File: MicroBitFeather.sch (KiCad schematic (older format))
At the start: 8 parts

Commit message: Wired some more things up.
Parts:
- added R?: 470, symbol R
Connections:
- net +5V: now also J?.1, U?.14 (VCC)
- net GND: now also J?.2, J?.MP (MountPin), U?.1 (~1OE), U?.10 (~3OE), U?.12 (4A), U?.13 (~4OE), U?.4 (~2OE), U?.5 (2A), U?.7 (GND), U?.9 (3A)
- net P1: now also U?.2 (1A)
- net at U?.3 (1Y): now also R?.1
- net at J?.2 (Pin_2): now also R?.2
- no-connect marks 1 -> 4
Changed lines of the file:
@@
 	1    0    0    -1
 $EndComp
+$Comp
+L +5V #PWR?
+U 1 1 5B87920C
+P 4700 4000
+F 0 "#PWR?" H 4700 3850 50  0001 C CNN
+F 1 "+5V" H 4700 4140 50  0000 C CNN
+F 2 "" H 4700 4000 50  0001 C CNN
+F 3 "" H 4700 4000 50  0001 C CNN
+	1    4700 4000
+	1    0    0    -1
+$EndComp
+$Comp
+L GND #PWR?
+U 1 1 5B879238
+P 4700 5600
+F 0 "#PWR?" H 4700 5350 50  0001 C CNN
+F 1 "GND" H 4700 5450 50  0000 C CNN
+F 2 "" H 4700 5600 50  0001 C CNN
+F 3 "" H 4700 5600 50  0001 C CNN
+	1    4700 5600
+	1    0    0    -1
+$EndComp
+Wire Wire Line
+	4700 4100 4700 4000
+Wire Wire Line
+	4700 5500 4700 5600
+$Comp
+L +5V #PWR?
+U 1 1 5B879F10
+P 4900 6000
+F 0 "#PWR?" H 4900 5850 50  0001 C CNN
+F 1 "+5V" H 4900 6140 50  0000 C CNN
+F 2 "" H 4900 6000 50  0001 C CNN
+F 3 "" H 4900 6000 50  0001 C CNN
+	1    4900 6000
+	1    0    0    -1
+$EndComp
+$Comp
+L GND #PWR?
+U 1 1 5B879F3C
+P 4500 6700
+F 0 "#PWR?" H 4500 6450 50  0001 C CNN
+F 1 "GND" H 4500 6550 50  0000 C CNN
+F 2 "" H 4500 6700 50  0001 C CNN
+F 3 "" H 4500 6700 50  0001 C CNN
+	1    4500 6700
+	1    0    0    -1
+$EndComp
+Wire Wire Line
+	4800 6100 4900 6100
+Wire Wire Line
+	4900 6100 4900 6000
+Wire Wire Line
+	4500 6500 4500 6700
+Wire Wire Line
+	4800 6300 5500 6300
+Wire Wire Line
+	5500 6300 5500 6600
+Wire Wire Line
+	5500 6600 4500 6600
+Connection ~ 4500 6600
+Wire Wire Line
+	5100 4300 5500 4300
+Wire Wire Line
+	5500 4800 6200 4800
+Wire Wire Line
+	4300 4400 4200 4400
+Wire Wire Line
+	4200 4400 4200 5550
+Wire Wire Line
+	4200 5550 4700 5550
+Connection ~ 4700 5550
+Wire Wire Line
+	4300 4600 4200 4600
+Connection ~ 4200 4600
+Wire Wire Line
+	4300 4700 4200 4700
+Connection ~ 4200 4700
+Wire Wire Line
+	4300 4900 4200 4900
+Connection ~ 4200 4900
+Wire Wire Line
+	4300 5000 4200 5000
+Connection ~ 4200 5000
+Wire Wire Line
+	4300 5200 4200 5200
+Connection ~ 4200 5200
+Wire Wire Line
+	4300 5300 4200 5300
+Connection ~ 4200 5300
+Text Label 4000 4300 0    50   ~ 0
+P1
+Wire Wire Line
+	4000 4300 4300 4300
+NoConn ~ 5100 4600
+NoConn ~ 5100 4900
+NoConn ~ 5100 5200
+$Comp
+L R R?
+U 1 1 5B87B000
+P 5500 4550
+F 0 "R?" V 5580 4550 50  0000 C CNN
+F 1 "470" V 5500 4550 50  0000 C CNN
+F 2 "" V 5430 4550 50  0001 C CNN
+F 3 "" H 5500 4550 50  0001 C CNN
+	1    5500 4550
+	1    0    0    -1
+$EndComp
+Wire Wire Line
+	5500 4300 5500 4400
+Wire Wire Line
+	5500 4700 5500 4800
 $EndSCHEMATC

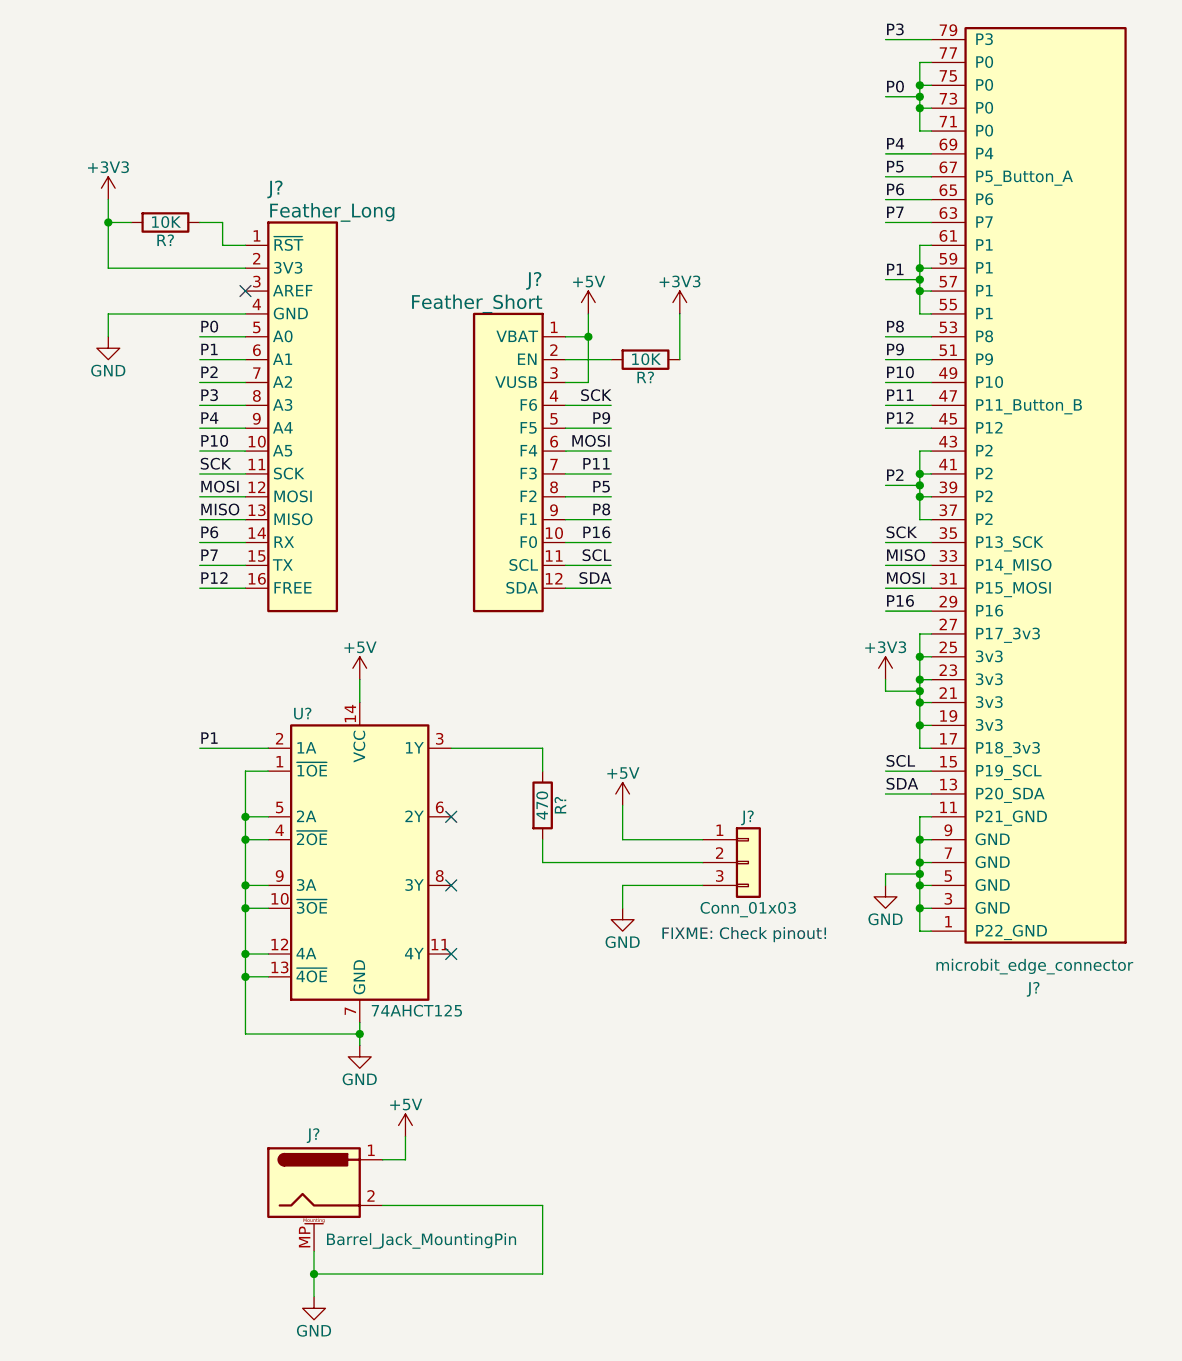
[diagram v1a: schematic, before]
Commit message: Add voltage regulator and more.
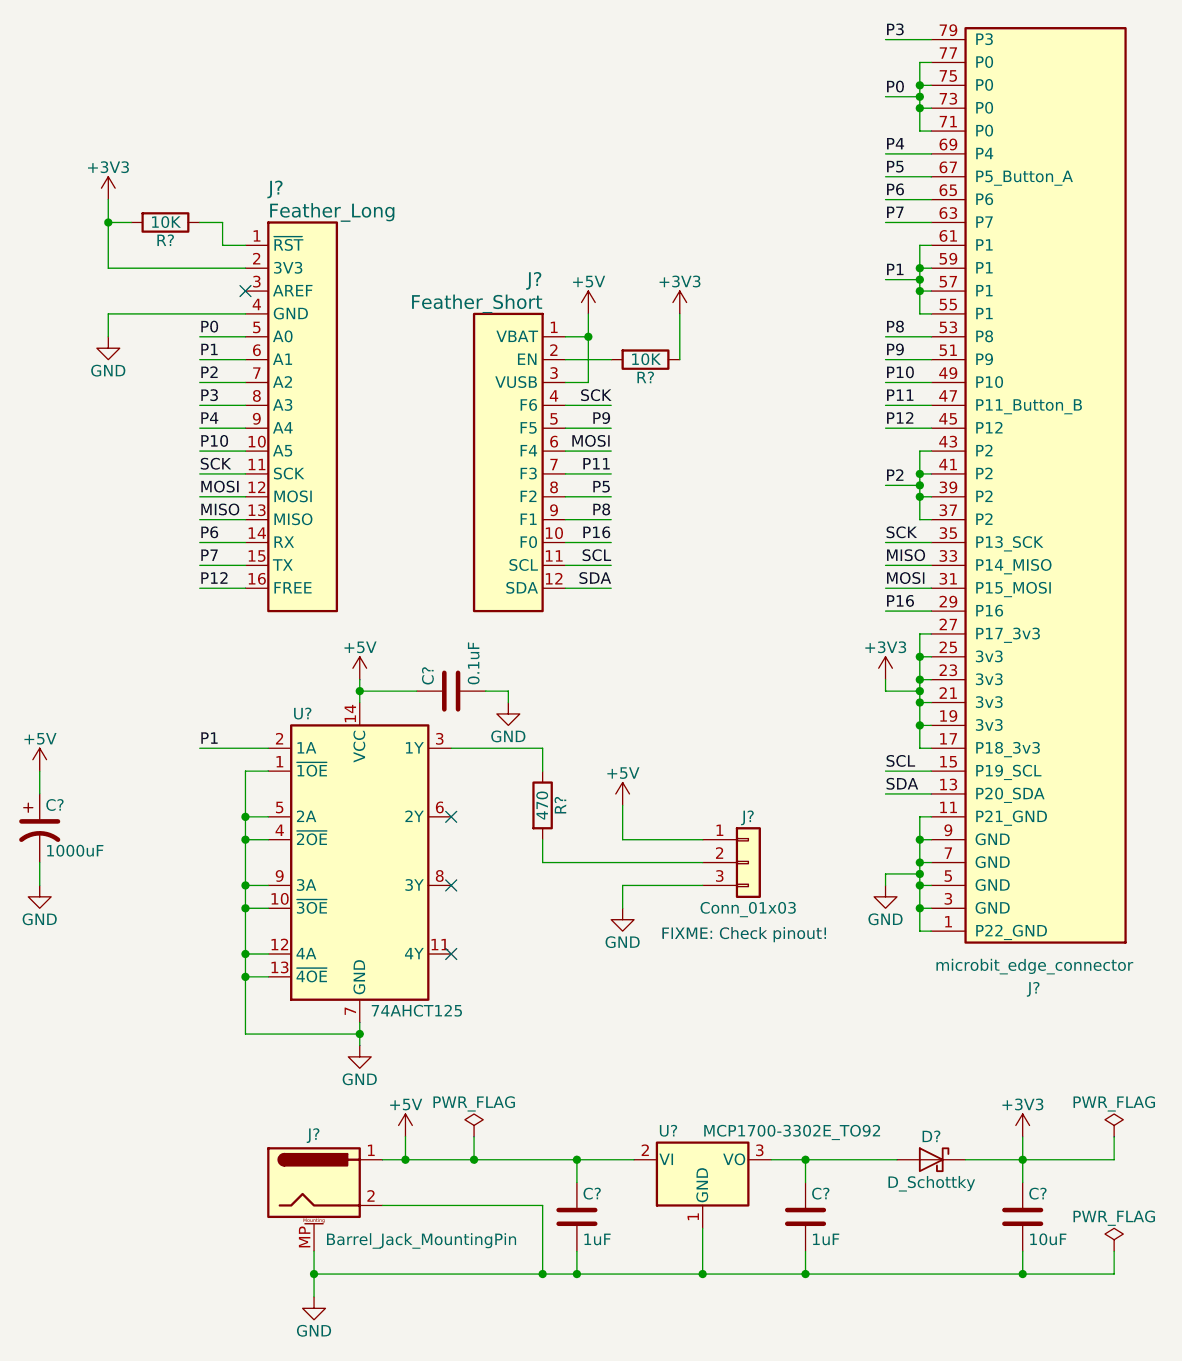
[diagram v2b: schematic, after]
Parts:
- added C? (x2): 1uF, symbol C
- added C?: 10uF, symbol C
- added C?: 0.1uF, symbol C
- added C?: 1000uF, symbol CP1
- added D?: D_Schottky, symbol D_Schottky
- added U?: MCP1700-3302E_TO92, TO_SOT_Packages_THT:TO-92_Inline_Narrow_Oval, symbol MCP1700-3302E_TO92
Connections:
- net +3V3: now also C?.1, D?.1 (K)
- net +5V: now also C?.1, C?.1, C?.1, U?.2 (VI)
- net GND: now also C?.2, C?.2, C?.2, C?.2, C?.2, U?.1 (GND)
- new net: C?.1, D?.2 (A), U?.3 (VO)
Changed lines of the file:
@@
 $EndComp
 Wire Wire Line
-	4800 6100 4900 6100
+	4800 6100 5900 6100
 Wire Wire Line
 	4900 6100 4900 6000
@@
 	5500 6300 5500 6600
 Wire Wire Line
-	5500 6600 4500 6600
+	4500 6600 8000 6600
 Connection ~ 4500 6600
 Wire Wire Line
@@
 Wire Wire Line
 	5500 4700 5500 4800
+$Comp
+L MCP1700-3302E_TO92 U?
+U 1 1 5B87B6E7
+P 6200 6100
+F 0 "U?" H 6050 5975 50  0000 C CNN
+F 1 "MCP1700-3302E_TO92" H 6200 5975 50  0000 L CNN
+F 2 "TO_SOT_Packages_THT:TO-92_Inline_Narrow_Oval" H 6200 5900 50  0001 C CIN
+F 3 "" H 6200 6100 50  0001 C CNN
+	1    6200 6100
+	1    0    0    1
+$EndComp
+$Comp
+L C C?
+U 1 1 5B87B8CD
+P 5650 6350
+F 0 "C?" H 5675 6450 50  0000 L CNN
+F 1 "1uF" H 5675 6250 50  0000 L CNN
+F 2 "" H 5688 6200 50  0001 C CNN
+F 3 "" H 5650 6350 50  0001 C CNN
+	1    5650 6350
+	1    0    0    -1
+$EndComp
+$Comp
+L C C?
+U 1 1 5B87B9B3
+P 6650 6350
+F 0 "C?" H 6675 6450 50  0000 L CNN
+F 1 "1uF" H 6675 6250 50  0000 L CNN
+F 2 "" H 6688 6200 50  0001 C CNN
+F 3 "" H 6650 6350 50  0001 C CNN
+	1    6650 6350
+	1    0    0    -1
+$EndComp
+Connection ~ 4900 6100
+Wire Wire Line
+	6650 6600 6650 6500
+Connection ~ 5500 6600
+Wire Wire Line
+	5650 6500 5650 6600
+Connection ~ 5650 6600
+Wire Wire Line
+	6200 6400 6200 6600
+Connection ~ 6200 6600
+$Comp
+L +3V3 #PWR?
+U 1 1 5B87BEFA
+P 7600 6000
+F 0 "#PWR?" H 7600 5850 50  0001 C CNN
+F 1 "+3V3" H 7600 6140 50  0000 C CNN
+F 2 "" H 7600 6000 50  0001 C CNN
+F 3 "" H 7600 6000 50  0001 C CNN
+	1    7600 6000
+	1    0    0    -1
+$EndComp
+Wire Wire Line
+	6500 6100 7050 6100
+Wire Wire Line
+	6650 6100 6650 6200
+$Comp
+L D_Schottky D?
+U 1 1 5B87C03F
+P 7200 6100
+F 0 "D?" H 7200 6200 50  0000 C CNN
+F 1 "D_Schottky" H 7200 6000 50  0000 C CNN
+F 2 "" H 7200 6100 50  0001 C CNN
+F 3 "" H 7200 6100 50  0001 C CNN
+	1    7200 6100
+	-1   0    0    -1
+$EndComp
+Connection ~ 6650 6100
+Wire Wire Line
+	7350 6100 8000 6100
+Wire Wire Line
+	7600 6000 7600 6200
+$Comp
+L C C?
+U 1 1 5B87C55E
+P 7600 6350
+F 0 "C?" H 7625 6450 50  0000 L CNN
+F 1 "10uF" H 7625 6250 50  0000 L CNN
+F 2 "" H 7638 6200 50  0001 C CNN
+F 3 "" H 7600 6350 50  0001 C CNN
+	1    7600 6350
+	1    0    0    -1
+$EndComp
+Connection ~ 7600 6100
+Wire Wire Line
+	7600 6600 7600 6500
+Connection ~ 6650 6600
+Wire Wire Line
+	5650 6200 5650 6100
+Connection ~ 5650 6100
+$Comp
+L C C?
+U 1 1 5B87CADC
+P 5100 4050
+F 0 "C?" H 5125 4150 50  0000 L CNN
+F 1 "0.1uF" H 5125 3950 50  0000 L CNN
+F 2 "" H 5138 3900 50  0001 C CNN
+F 3 "" H 5100 4050 50  0001 C CNN
+	1    5100 4050
+	0    -1   -1   0
+$EndComp
+$Comp
+L GND #PWR?
+U 1 1 5B87CC46
+P 5350 4100
+F 0 "#PWR?" H 5350 3850 50  0001 C CNN
+F 1 "GND" H 5350 3950 50  0000 C CNN
+F 2 "" H 5350 4100 50  0001 C CNN
+F 3 "" H 5350 4100 50  0001 C CNN
+	1    5350 4100
+	1    0    0    -1
+$EndComp
+Wire Wire Line
+	4700 4050 4950 4050
+Connection ~ 4700 4050
+Wire Wire Line
+	5250 4050 5350 4050
+Wire Wire Line
+	5350 4050 5350 4100
+$Comp
+L CP1 C?
+U 1 1 5B87D36C
+P 3300 4650
+F 0 "C?" H 3325 4750 50  0000 L CNN
+F 1 "1000uF" H 3325 4550 50  0000 L CNN
+F 2 "" H 3300 4650 50  0001 C CNN
+F 3 "" H 3300 4650 50  0001 C CNN
+	1    3300 4650
+	1    0    0    -1
+$EndComp
+$Comp
+L GND #PWR?
+U 1 1 5B87D3B2
+P 3300 4900
+F 0 "#PWR?" H 3300 4650 50  0001 C CNN
+F 1 "GND" H 3300 4750 50  0000 C CNN
+F 2 "" H 3300 4900 50  0001 C CNN
+F 3 "" H 3300 4900 50  0001 C CNN
+	1    3300 4900
+	1    0    0    -1
+$EndComp
+$Comp
+L +5V #PWR?
+U 1 1 5B87D3F6
+P 3300 4400
+F 0 "#PWR?" H 3300 4250 50  0001 C CNN
+F 1 "+5V" H 3300 4540 50  0000 C CNN
+F 2 "" H 3300 4400 50  0001 C CNN
+F 3 "" H 3300 4400 50  0001 C CNN
+	1    3300 4400
+	1    0    0    -1
+$EndComp
+Wire Wire Line
+	3300 4500 3300 4400
+Wire Wire Line
+	3300 4800 3300 4900
+$Comp
+L PWR_FLAG #FLG?
+U 1 1 5B87DB70
+P 5200 6000
+F 0 "#FLG?" H 5200 6075 50  0001 C CNN
+F 1 "PWR_FLAG" H 5200 6150 50  0000 C CNN
+F 2 "" H 5200 6000 50  0001 C CNN
+F 3 "" H 5200 6000 50  0001 C CNN
+	1    5200 6000
+	1    0    0    -1
+$EndComp
+$Comp
+L PWR_FLAG #FLG?
+U 1 1 5B87DBB4
+P 8000 6000
+F 0 "#FLG?" H 8000 6075 50  0001 C CNN
+F 1 "PWR_FLAG" H 8000 6150 50  0000 C CNN
+F 2 "" H 8000 6000 50  0001 C CNN
+F 3 "" H 8000 6000 50  0001 C CNN
+	1    8000 6000
+	1    0    0    -1
+$EndComp
+$Comp
+L PWR_FLAG #FLG?
+U 1 1 5B87DBF8
+P 8000 6500
+F 0 "#FLG?" H 8000 6575 50  0001 C CNN
+F 1 "PWR_FLAG" H 8000 6650 50  0000 C CNN
+F 2 "" H 8000 6500 50  0001 C CNN
+F 3 "" H 8000 6500 50  0001 C CNN
+	1    8000 6500
+	1    0    0    -1
+$EndComp
+Wire Wire Line
+	5200 6000 5200 6100
+Connection ~ 5200 6100
+Wire Wire Line
+	8000 6100 8000 6000
+Wire Wire Line
+	8000 6600 8000 6500
+Connection ~ 7600 6600
 $EndSCHEMATC

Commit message: Fill in manufacturer part numbers.
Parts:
- removed C?: 1uF, symbol C
- removed R?: 10K, symbol R
- added C?: 1uF, symbol C
- added R?: 10K, symbol R
- C?: Description (none) -> CAP CER 1UF 50V Y5V RADIAL; Digi-Key_PN (none) -> BC1168CT-ND; MPN (none) -> K105Z20Y5VF5TH5
- C?: value 10uF -> 100uF; Description (none) -> CAP ALUM 100UF 20% 10V RADIAL; Digi-Key_PN (none) -> P963-ND; MPN (none) -> ECE-A1AKS101
- C?: Description (none) -> CAP CER 0.1UF 50V X7R RADIAL; Digi-Key_PN (none) -> BC2665CT-ND; MPN (none) -> K104K10X7RF5UH5
- C?: Description (none) -> CAP ALUM 1000UF 20% 10V RADIAL; Digi-Key_PN (none) -> 1189-3703-1-ND; MPN (none) -> 10WXA1000MEFCT810X9
- D?: Description (none) -> DIODE SCHOTTKY 40V 2A DO15; Digi-Key_PN (none) -> 1655-1519-1-ND; MPN (none) -> SB240TA
- J?: Description (none) -> micro:bit through-hole right-angle edge connector; MPN (none) -> 3342
- J?: Description (none) -> CONN HEADER FMALE 16POS .1\" GOLD; Digi-Key_PN (none) -> S7049-ND; MPN (none) -> PPPC161LFBN-RC
- J?: Description (none) -> CONN HEADER FMALE 12POS .1\" GOLD; Digi-Key_PN (none) -> S7045-ND; MPN (none) -> PPPC121LFBN-RC
- J?: Description (none) -> CONN PWR JACK 2X5.5MM SOLDER; Digi-Key_PN (none) -> CP-063AH-ND; MPN (none) -> PJ-063AH
- J?: value Conn_01x03 -> NeoPixels; Description (none) -> CONN HEADER PH SIDE 3POS 2MM; Digi-Key_PN (none) -> 455-1720-ND; MPN (none) -> S3B-PH-K-S(LF)(SN)
- R?: Description (none) -> RES 10K OHM 1/4W 5% AXIAL; Digi-Key_PN (none) -> CF14JT10K0CT-ND; MPN (none) -> CF14JT10K0
- R?: Description (none) -> RES 470 OHM 1/4W 5% AXIAL; Digi-Key_PN (none) -> CF14JT470RCT-ND; MPN (none) -> CF14JT470R
- U?: Description (none) -> IC BUF NON-INVERT 5.5V 14DIP; Digi-Key_PN (none) -> 296-4655-5-ND; MPN (none) -> SN74AHCT125N
- U?: value MCP1700-3302E_TO92 -> MCP1702-3302E_TO92; Description (none) -> IC REG LINEAR 3.3V 250MA TO92-3; Digi-Key_PN (none) -> MCP1702-3302E/TO-ND; MPN (none) -> MCP1702-3302E/TO
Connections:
- net +3V3: now also R?.1
- net GND: now also C?.2
- net at J?.2 (EN): now also R?.2
- net at D?.2 (A), U?.3 (VO): now also C?.1
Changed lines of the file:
@@
 F 2 "" H 7600 3200 50  0001 C CNN
 F 3 "" H 7600 3200 50  0001 C CNN
+F 4 "3342" H 7700 3300 60  0001 C CNN "MPN"
+F 5 "micro:bit through-hole right-angle edge connector" H 7700 3300 60  0001 C CNN "Description"
 	1    7700 3300
 	-1   0    0    1
@@
 F 2 "" H 4200 2100 60  0001 C CNN
 F 3 "" H 4200 2100 60  0001 C CNN
+F 4 "PPPC161LFBN-RC" H 4200 2100 60  0001 C CNN "MPN"
+F 5 "CONN HEADER FMALE 16POS .1\" GOLD" H 4200 2100 60  0001 C CNN "Description"
+F 6 "S7049-ND" H 4200 2100 60  0001 C CNN "Digi-Key_PN"
 	1    4200 2100
 	1    0    0    -1
@@
 F 2 "" H 5600 2500 60  0001 C CNN
 F 3 "" H 5600 2500 60  0001 C CNN
+F 4 "PPPC121LFBN-RC" H 5600 2500 60  0001 C CNN "MPN"
+F 5 "CONN HEADER FMALE 12POS .1\" GOLD" H 5600 2500 60  0001 C CNN "Description"
+F 6 "S7045-ND" H 5600 2500 60  0001 C CNN "Digi-Key_PN"
 	1    5600 2500
 	-1   0    0    -1
@@
 F 2 "" V 3780 2000 50  0001 C CNN
 F 3 "" H 3850 2000 50  0001 C CNN
+F 4 "CF14JT10K0" H 3850 2000 60  0001 C CNN "MPN"
+F 5 "RES 10K OHM 1/4W 5% AXIAL" H 3850 2000 60  0001 C CNN "Description"
+F 6 "CF14JT10K0CT-ND" H 3850 2000 60  0001 C CNN "Digi-Key_PN"
 	1    3850 2000
 	0    1    1    0
@@
 	4000 3600 4200 3600
 $Comp
-L R R?
-U 1 1 5B878A2A
-P 5950 2600
-F 0 "R?" V 6030 2600 50  0000 C CNN
-F 1 "10K" V 5950 2600 50  0000 C CNN
-F 2 "" V 5880 2600 50  0001 C CNN
-F 3 "" H 5950 2600 50  0001 C CNN
-	1    5950 2600
-	0    1    1    0
-$EndComp
-$Comp
 L +3V3 #PWR?
 U 1 1 5B878A64
@@
 P 6400 4800
 F 0 "J?" H 6400 5000 50  0000 C CNN
-F 1 "Conn_01x03" H 6400 4600 50  0000 C CNN
+F 1 "NeoPixels" H 6400 4600 50  0000 C CNN
 F 2 "" H 6400 4800 50  0001 C CNN
 F 3 "" H 6400 4800 50  0001 C CNN
+F 4 "S3B-PH-K-S(LF)(SN)" H 6400 4800 60  0001 C CNN "MPN"
+F 5 "CONN HEADER PH SIDE 3POS 2MM" H 6400 4800 60  0001 C CNN "Description"
+F 6 "455-1720-ND" H 6400 4800 60  0001 C CNN "Digi-Key_PN"
 	1    6400 4800
 	1    0    0    -1
@@
 F 2 "" H 4700 4800 60  0000 C CNN
 F 3 "" H 4700 4800 60  0000 C CNN
+F 4 "SN74AHCT125N" H 4700 4800 60  0001 C CNN "MPN"
+F 5 "IC BUF NON-INVERT 5.5V 14DIP" H 4700 4800 60  0001 C CNN "Description"
+F 6 "296-4655-5-ND" H 4700 4800 60  0001 C CNN "Digi-Key_PN"
 	1    4700 4800
 	1    0    0    -1
@@
 F 2 "" H 4550 6160 50  0001 C CNN
 F 3 "" H 4550 6160 50  0001 C CNN
+F 4 "PJ-063AH" H 4500 6200 60  0001 C CNN "MPN"
+F 5 "CONN PWR JACK 2X5.5MM SOLDER" H 4500 6200 60  0001 C CNN "Description"
+F 6 "CP-063AH-ND" H 4500 6200 60  0001 C CNN "Digi-Key_PN"
 	1    4500 6200
 	1    0    0    -1
@@
 F 2 "" V 5430 4550 50  0001 C CNN
 F 3 "" H 5500 4550 50  0001 C CNN
+F 4 "CF14JT470R" H 5500 4550 60  0001 C CNN "MPN"
+F 5 "RES 470 OHM 1/4W 5% AXIAL" H 5500 4550 60  0001 C CNN "Description"
+F 6 "CF14JT470RCT-ND" H 5500 4550 60  0001 C CNN "Digi-Key_PN"
 	1    5500 4550
 	1    0    0    -1
@@
 P 6200 6100
 F 0 "U?" H 6050 5975 50  0000 C CNN
-F 1 "MCP1700-3302E_TO92" H 6200 5975 50  0000 L CNN
+F 1 "MCP1702-3302E_TO92" H 6200 5975 50  0000 L CNN
 F 2 "TO_SOT_Packages_THT:TO-92_Inline_Narrow_Oval" H 6200 5900 50  0001 C CIN
 F 3 "" H 6200 6100 50  0001 C CNN
+F 4 "MCP1702-3302E/TO" H 6200 6100 60  0001 C CNN "MPN"
+F 5 "IC REG LINEAR 3.3V 250MA TO92-3" H 6200 6100 60  0001 C CNN "Description"
+F 6 "MCP1702-3302E/TO-ND" H 6200 6100 60  0001 C CNN "Digi-Key_PN"
 	1    6200 6100
 	1    0    0    1
@@
 F 2 "" H 5688 6200 50  0001 C CNN
 F 3 "" H 5650 6350 50  0001 C CNN
+F 4 "K105Z20Y5VF5TH5" H 5650 6350 60  0001 C CNN "MPN"
+F 5 "CAP CER 1UF 50V Y5V RADIAL" H 5650 6350 60  0001 C CNN "Description"
+F 6 "BC1168CT-ND" H 5650 6350 60  0001 C CNN "Digi-Key_PN"
 	1    5650 6350
-	1    0    0    -1
-$EndComp
-$Comp
-L C C?
-U 1 1 5B87B9B3
-P 6650 6350
-F 0 "C?" H 6675 6450 50  0000 L CNN
-F 1 "1uF" H 6675 6250 50  0000 L CNN
-F 2 "" H 6688 6200 50  0001 C CNN
-F 3 "" H 6650 6350 50  0001 C CNN
-	1    6650 6350
 	1    0    0    -1
 $EndComp
@@
 F 2 "" H 7200 6100 50  0001 C CNN
 F 3 "" H 7200 6100 50  0001 C CNN
+F 4 "SB240TA" H 7200 6100 60  0001 C CNN "MPN"
+F 5 "DIODE SCHOTTKY 40V 2A DO15" H 7200 6100 60  0001 C CNN "Description"
+F 6 "1655-1519-1-ND" H 7200 6100 60  0001 C CNN "Digi-Key_PN"
 	1    7200 6100
 	-1   0    0    -1
@@
 P 7600 6350
 F 0 "C?" H 7625 6450 50  0000 L CNN
-F 1 "10uF" H 7625 6250 50  0000 L CNN
+F 1 "100uF" H 7625 6250 50  0000 L CNN
 F 2 "" H 7638 6200 50  0001 C CNN
 F 3 "" H 7600 6350 50  0001 C CNN
+F 4 "ECE-A1AKS101" H 7600 6350 60  0001 C CNN "MPN"
+F 5 "CAP ALUM 100UF 20% 10V RADIAL" H 7600 6350 60  0001 C CNN "Description"
+F 6 "P963-ND" H 7600 6350 60  0001 C CNN "Digi-Key_PN"
 	1    7600 6350
 	1    0    0    -1
@@
 F 2 "" H 5138 3900 50  0001 C CNN
 F 3 "" H 5100 4050 50  0001 C CNN
+F 4 "K104K10X7RF5UH5" H 5100 4050 60  0001 C CNN "MPN"
+F 5 "CAP CER 0.1UF 50V X7R RADIAL" H 5100 4050 60  0001 C CNN "Description"
+F 6 "BC2665CT-ND" H 5100 4050 60  0001 C CNN "Digi-Key_PN"
 	1    5100 4050
 	0    -1   -1   0
@@
 F 2 "" H 3300 4650 50  0001 C CNN
 F 3 "" H 3300 4650 50  0001 C CNN
+F 4 "10WXA1000MEFCT810X9" H 3300 4650 60  0001 C CNN "MPN"
+F 5 "CAP ALUM 1000UF 20% 10V RADIAL" H 3300 4650 60  0001 C CNN "Description"
+F 6 "1189-3703-1-ND" H 3300 4650 60  0001 C CNN "Digi-Key_PN"
 	1    3300 4650
 	1    0    0    -1
@@
 	8000 6600 8000 6500
 Connection ~ 7600 6600
+$Comp
+L C C?
+U 1 1 5B888051
+P 6650 6350
+F 0 "C?" H 6675 6450 50  0000 L CNN
+F 1 "1uF" H 6675 6250 50  0000 L CNN
+F 2 "" H 6688 6200 50  0001 C CNN
+F 3 "" H 6650 6350 50  0001 C CNN
+F 4 "K105Z20Y5VF5TH5" H 6650 6350 60  0001 C CNN "MPN"
+F 5 "CAP CER 1UF 50V Y5V RADIAL" H 6650 6350 60  0001 C CNN "Description"
+F 6 "BC1168CT-ND" H 6650 6350 60  0001 C CNN "Digi-Key_PN"
+	1    6650 6350
+	1    0    0    -1
+$EndComp
+$Comp
+L R R?
+U 1 1 5B88A204
+P 5950 2600
+F 0 "R?" V 6030 2600 50  0000 C CNN
+F 1 "10K" V 5950 2600 50  0000 C CNN
+F 2 "" V 5880 2600 50  0001 C CNN
+F 3 "" H 5950 2600 50  0001 C CNN
+F 4 "CF14JT10K0" H 5950 2600 60  0001 C CNN "MPN"
+F 5 "RES 10K OHM 1/4W 5% AXIAL" H 5950 2600 60  0001 C CNN "Description"
+F 6 "CF14JT10K0CT-ND" H 5950 2600 60  0001 C CNN "Digi-Key_PN"
+	1    5950 2600
+	0    1    1    0
+$EndComp
 $EndSCHEMATC
